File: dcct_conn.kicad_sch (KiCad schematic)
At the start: 1 part, among them J8 1731130154

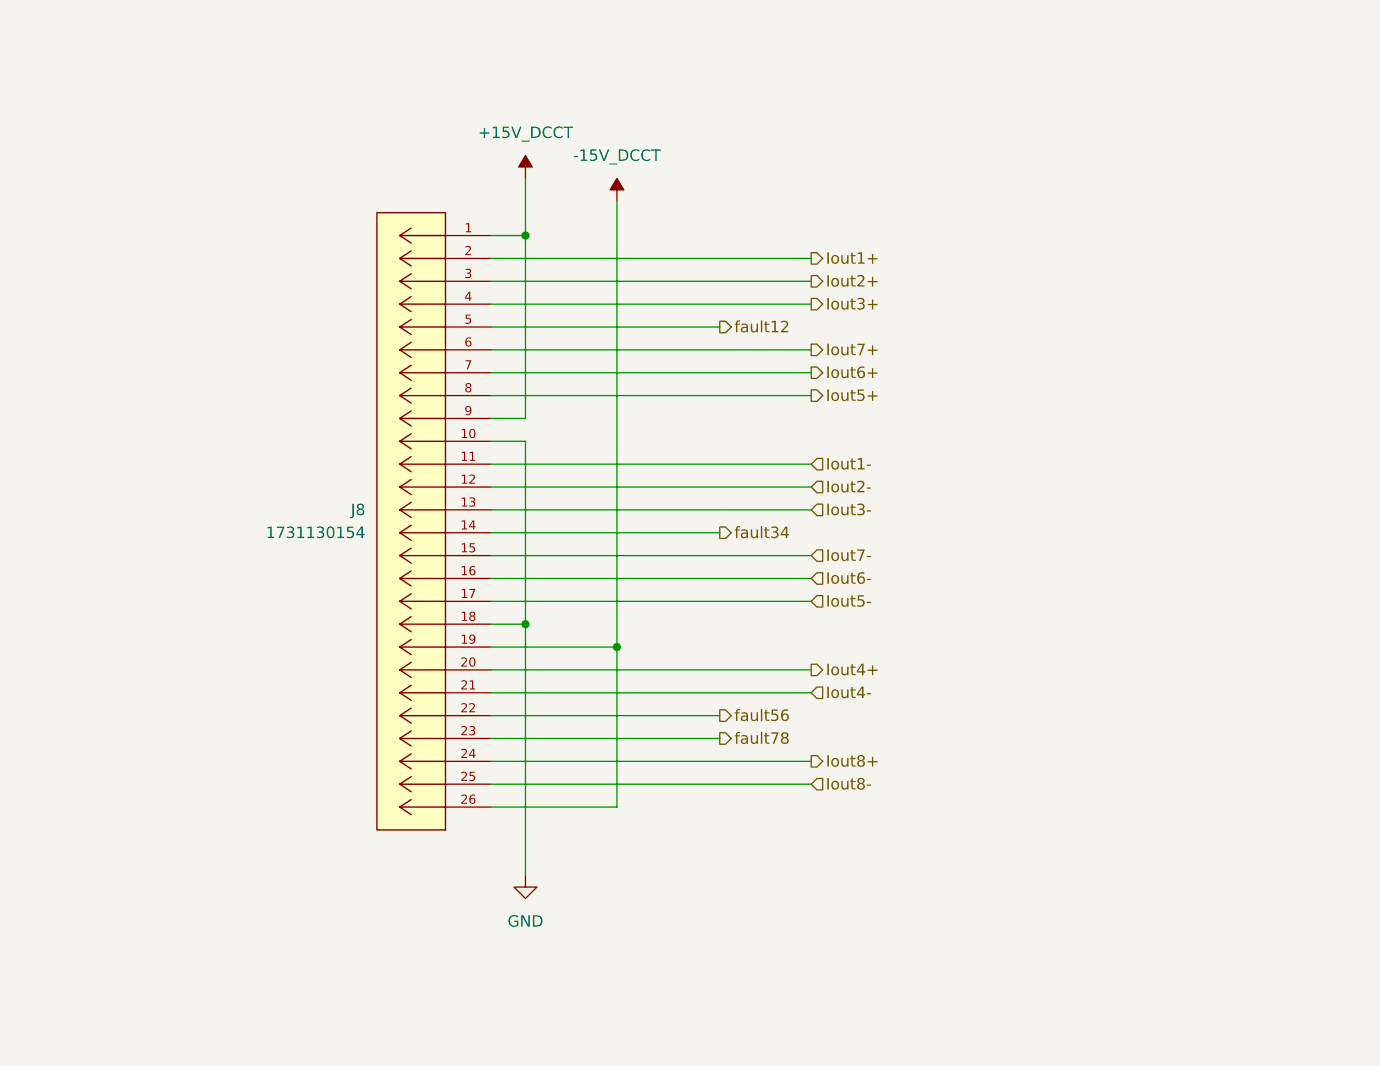
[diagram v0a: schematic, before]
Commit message: Add all 4 channels
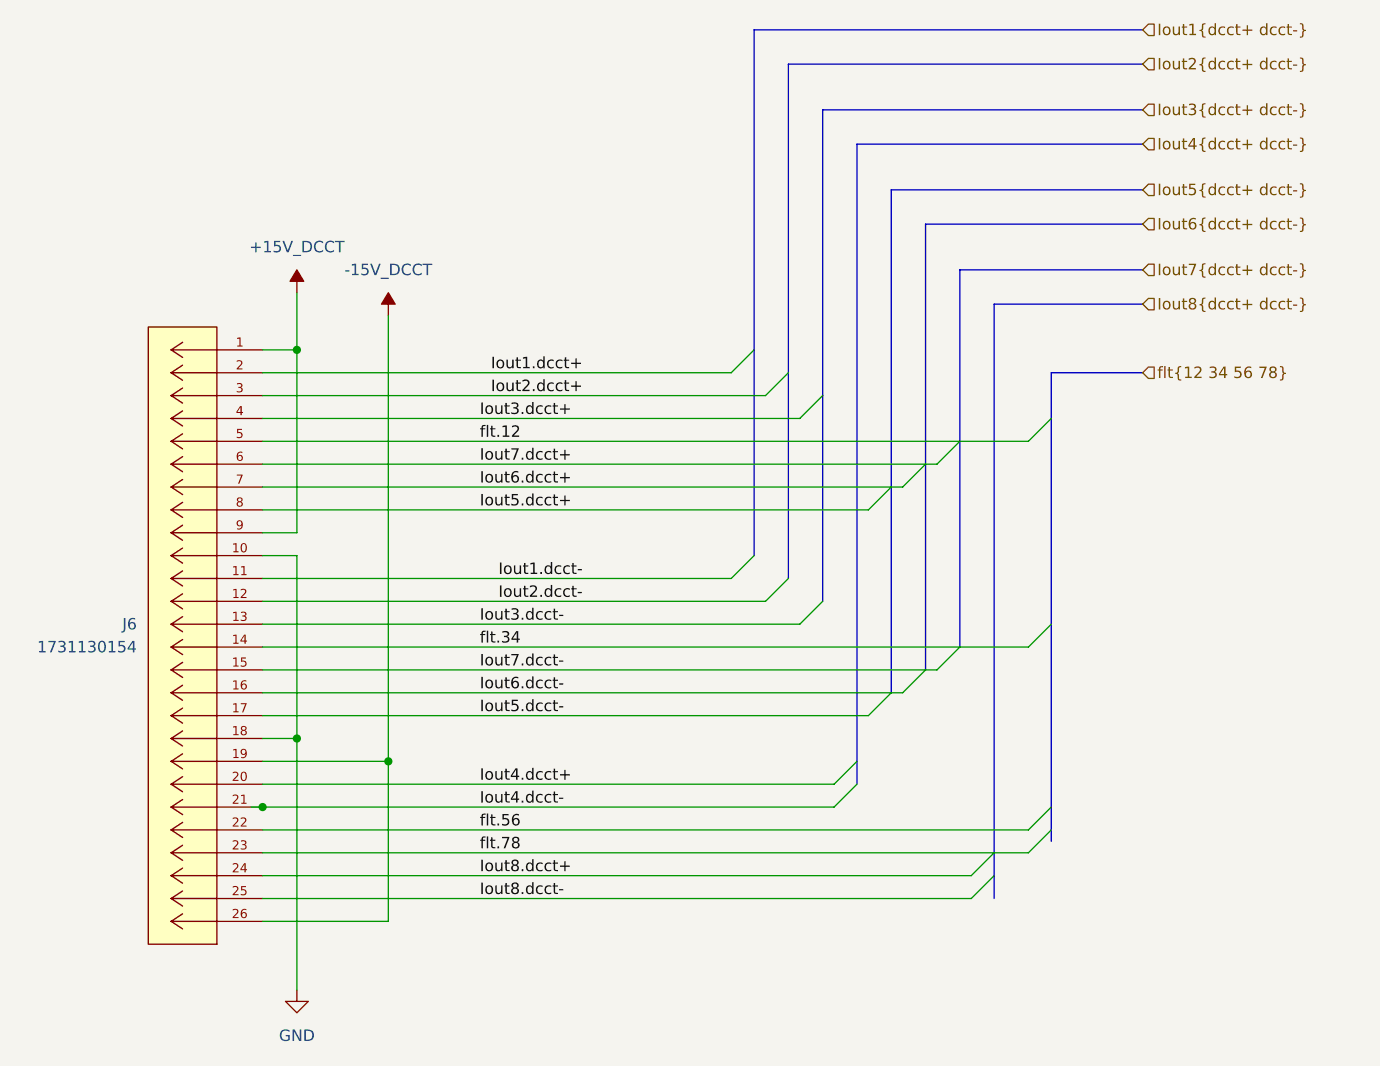
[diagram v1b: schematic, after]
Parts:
- renumbered J8 to J6
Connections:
- net Iout1+ renamed Iout1.dcct+
- net Iout1- renamed Iout1.dcct-
- net Iout2+ renamed Iout2.dcct+
- net Iout2- renamed Iout2.dcct-
- net Iout3+ renamed Iout3.dcct+
- net Iout3- renamed Iout3.dcct-
- net Iout4+ renamed Iout4.dcct+
- net Iout4- renamed Iout4.dcct-
- net Iout5+ renamed Iout5.dcct+
- net Iout5- renamed Iout5.dcct-
- net Iout6+ renamed Iout6.dcct+
- net Iout6- renamed Iout6.dcct-
- net Iout7+ renamed Iout7.dcct+
- net Iout7- renamed Iout7.dcct-
- net Iout8+ renamed Iout8.dcct+
- net Iout8- renamed Iout8.dcct-
- net fault12 renamed flt.12
- net fault34 renamed flt.34
- net fault56 renamed flt.56
- net fault78 renamed flt.78
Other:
- moved on the sheet: J6

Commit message: Start routing
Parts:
- renumbered J6 to J7
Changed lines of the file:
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@@
-	)
-	(junction
-		(at 90.17 125.73)
-		(diameter 0)
-		(color 0 0 0 0)
 	)
 	(junction
@@
 	(wire
 		(pts
-			(xy 88.9 125.73) (xy 90.17 125.73)
-		)
-		(stroke
-			(width 0)
-			(type default)
-		)
-	)
-	(wire
-		(pts
 			(xy 90.17 77.47) (xy 142.24 77.47)
 		)
@@
 	(wire
 		(pts
+			(xy 90.17 85.09) (xy 167.64 85.09)
+		)
+		(stroke
+			(width 0)
+			(type default)
+		)
+	)
+	(wire
+		(pts
 			(xy 104.14 71.12) (xy 104.14 120.65)
 		)
@@
 	(wire
 		(pts
+			(xy 90.17 125.73) (xy 153.67 125.73)
+		)
+		(stroke
+			(width 0)
+			(type default)
+		)
+	)
+	(wire
+		(pts
 			(xy 90.17 107.95) (xy 167.64 107.95)
 		)
@@
 	(wire
 		(pts
-			(xy 90.17 125.73) (xy 153.67 125.73)
+			(xy 167.64 85.09) (xy 175.26 85.09)
 		)
 		(stroke
@@
 	(wire
 		(pts
-			(xy 90.17 85.09) (xy 167.64 85.09)
-		)
-		(stroke
-			(width 0)
-			(type default)
-		)
-	)
-	(wire
-		(pts
 			(xy 104.14 120.65) (xy 90.17 120.65)
 		)
@@
 		(pts
 			(xy 171.45 130.81) (xy 175.26 130.81)
-		)
-		(stroke
-			(width 0)
-			(type default)
-		)
-	)
-	(wire
-		(pts
-			(xy 167.64 85.09) (xy 175.26 85.09)
 		)
 		(stroke
@@
 		(on_board yes)
 		(dnp no)
-		(property "Reference" "J6"
+		(property "Reference" "J7"
 			(at 76.2 105.4099 0)
 			(effects
@@
 			(project "psc_carrier_brd"
 				(path "/40891cc8-bf64-41f4-8f69-a607d7b280eb/ee7775f8-818d-4b39-ac35-648c0c49495f"
-					(reference "J6")
+					(reference "J7")
 					(unit 1)
 				)
@@
 		(dnp no)
 		(fields_autoplaced yes)
-		(property "Reference" "#PWR030"
+		(property "Reference" "#PWR031"
 			(at 93.98 152.4 0)
 			(effects
@@
 			(project ""
 				(path "/40891cc8-bf64-41f4-8f69-a607d7b280eb/ee7775f8-818d-4b39-ac35-648c0c49495f"
-					(reference "#PWR030")
+					(reference "#PWR031")
 					(unit 1)
 				)
@@
 		(dnp no)
 		(fields_autoplaced yes)
-		(property "Reference" "#PWR031"
+		(property "Reference" "#PWR032"
 			(at 104.14 74.93 0)
 			(effects
@@
 			(project ""
 				(path "/40891cc8-bf64-41f4-8f69-a607d7b280eb/ee7775f8-818d-4b39-ac35-648c0c49495f"
-					(reference "#PWR031")
+					(reference "#PWR032")
 					(unit 1)
 				)
@@
 		(dnp no)
 		(fields_autoplaced yes)
-		(property "Reference" "#PWR029"
+		(property "Reference" "#PWR030"
 			(at 93.98 72.39 0)
 			(effects
@@
 			(project ""
 				(path "/40891cc8-bf64-41f4-8f69-a607d7b280eb/ee7775f8-818d-4b39-ac35-648c0c49495f"
-					(reference "#PWR029")
+					(reference "#PWR030")
 					(unit 1)
 				)

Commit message: Finished layout
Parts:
- J7: Cost (none) -> 24.50; MFG (none) -> Molex; MFG_PN (none) -> 1731130154
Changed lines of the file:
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@@
 			)
 		)
-		(property "Description" ""
+		(property "Description" "CONN D-SUB HD PLG 26POS R/A SLDR"
 			(at 90.17 74.93 0)
 			(effects
@@
 				(hide yes)
 			)
+		)
+		(property "Cost" "24.50"
+			(at 90.17 74.93 0)
+			(effects
+				(font
+					(size 1.27 1.27)
+				)
+				(hide yes)
+			)
+		)
+		(property "MFG" "Molex"
+			(at 90.17 74.93 0)
+			(effects
+				(font
+					(size 1.27 1.27)
+				)
+				(hide yes)
+			)
+		)
+		(property "MFG_PN" "1731130154"
+			(at 90.17 74.93 0)
+			(effects
+				(font
+					(size 1.27 1.27)
+				)
+				(hide yes)
+			)
